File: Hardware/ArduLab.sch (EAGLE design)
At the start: 94 parts, among them CN1 USB-B, CN2 JST-PH, Q1 BSS138, Q2 BSS138, U1 ATMEGA32U4-AU, U2 MIC5205, U3 PAM2401, U4 MCP73831, U5 L293DD, U6 HC_05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

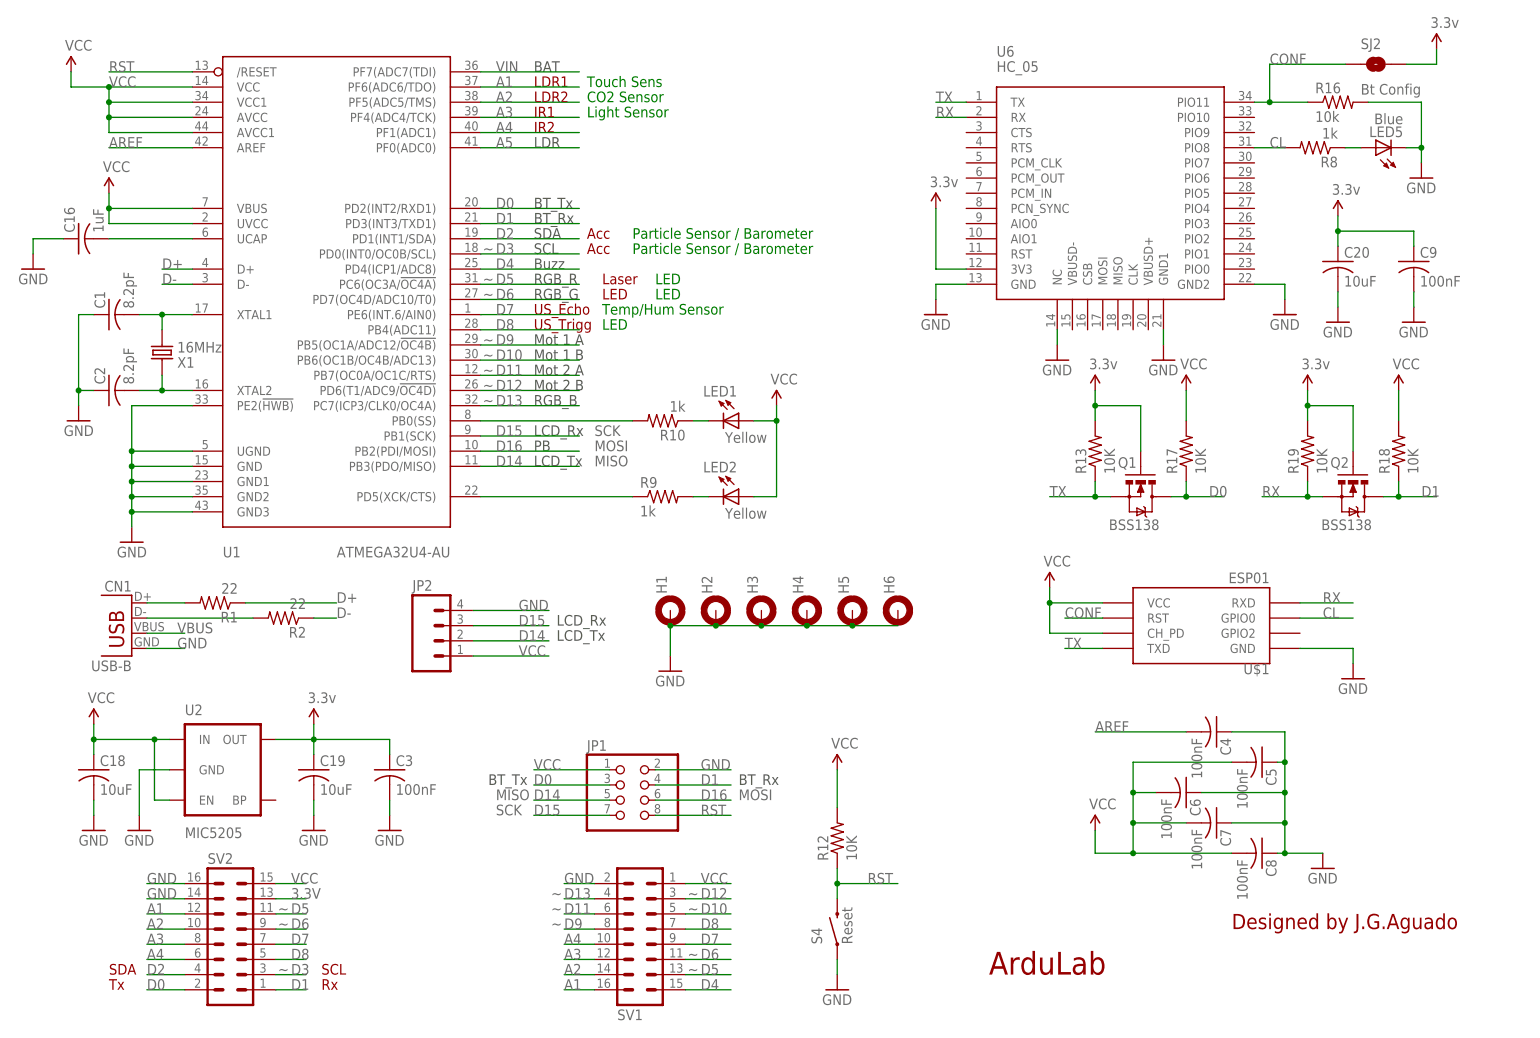
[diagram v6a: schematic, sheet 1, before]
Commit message: 2.4GHz RF ML01D Module Integration
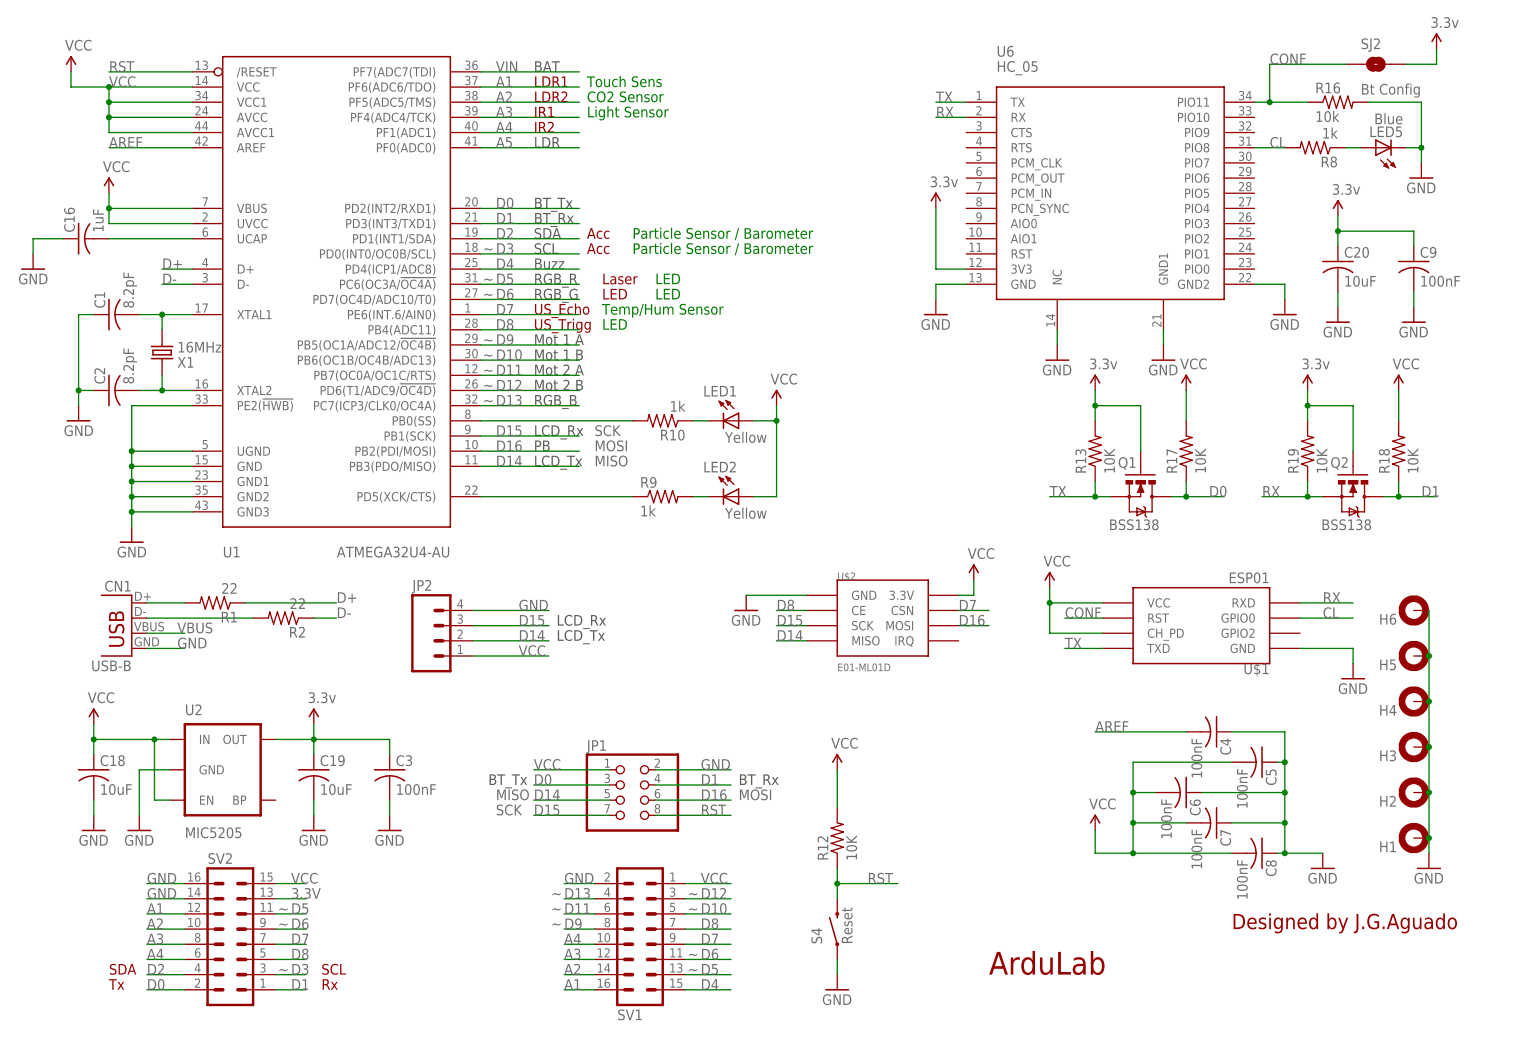
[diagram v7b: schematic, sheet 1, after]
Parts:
- added U$2: E01-ML01D, SpaceDIY_connectors:E01-ML01D
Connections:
- net 3.3V: now also U$2.3.3V
- net D14: now also U$2.MISO
- net D15: now also U$2.SCK
- net D16: now also U$2.MOSI
- net D7: now also U$2.CSN
- net D8: now also U$2.CE
- net GND: now also U$2.GND
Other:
- moved on the sheet: H1, H2, H3, H4, H5, H6
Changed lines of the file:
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@@
 <setting verticaltext="up"/>
 </settings>
-<grid distance="0.1" unitdist="inch" unit="inch" style="lines" multiple="1" display="no" altdistance="0.01" altunitdist="inch" altunit="inch"/>
+<grid distance="0.05" unitdist="inch" unit="inch" style="lines" multiple="1" display="no" altdistance="0.01" altunitdist="inch" altunit="inch"/>
 <layers>
 <layer number="1" name="Top" color="4" fill="1" visible="no" active="no"/>
@@
 <part name="GND5" library="SparkFun" deviceset="GND" device=""/>
 <part name="F1" library="adafruit" deviceset="PTCFUSE" device="-1206" value="500mA"/>
+<part name="GND7" library="SparkFun" deviceset="GND" device=""/>
+<part name="P+12" library="SparkFun" deviceset="3.3V" device="" value="VCC"/>
+<part name="U$2" library="SpaceDIY_connectors" deviceset="E01-ML01D" device=""/>
 </parts>
 <sheets>
@@
 <instance part="R2" gate="G$1" x="57.15" y="72.39" rot="R180"/>
 <instance part="CN1" gate="G$1" x="31.75" y="67.31" rot="MR0"/>
-<instance part="H1" gate="G$1" x="121.92" y="73.66" rot="R90"/>
-<instance part="H2" gate="G$1" x="129.54" y="73.66" rot="R90"/>
-<instance part="H3" gate="G$1" x="137.16" y="73.66" rot="R90"/>
-<instance part="H4" gate="G$1" x="144.78" y="73.66" rot="R90"/>
-<instance part="GND34" gate="1" x="121.92" y="63.5"/>
+<instance part="H1" gate="G$1" x="246.38" y="35.56" rot="R180"/>
+<instance part="H2" gate="G$1" x="246.38" y="43.18" rot="R180"/>
+<instance part="H3" gate="G$1" x="246.38" y="50.8" rot="R180"/>
+<instance part="H4" gate="G$1" x="246.38" y="58.42" rot="R180"/>
+<instance part="GND34" gate="1" x="248.92" y="30.48"/>
 <instance part="R16" gate="G$1" x="233.68" y="158.75"/>
 <instance part="R8" gate="G$1" x="229.87" y="151.13" rot="R180"/>
@@
 <instance part="3.3V4" gate="G$1" x="62.23" y="54.61"/>
 <instance part="P+9" gate="G$1" x="25.4" y="54.61"/>
-<instance part="H5" gate="G$1" x="152.4" y="73.66" rot="R90"/>
-<instance part="H6" gate="G$1" x="160.02" y="73.66" rot="R90"/>
+<instance part="H5" gate="G$1" x="246.38" y="66.04" rot="R180"/>
+<instance part="H6" gate="G$1" x="246.38" y="73.66" rot="R180"/>
 <instance part="C19" gate="G$1" x="62.23" y="46.99"/>
 <instance part="C18" gate="G$1" x="25.4" y="46.99"/>
@@
 <instance part="GND46" gate="1" x="204.47" y="115.57"/>
 <instance part="U1" gate="G$1" x="64.77" y="120.65"/>
+<instance part="GND7" gate="1" x="134.62" y="73.66"/>
+<instance part="P+12" gate="G$1" x="172.72" y="78.74"/>
+<instance part="U$2" gate="G$1" x="157.48" y="66.04"/>
 </instances>
 <busses>
@@
 </segment>
 <segment>
-<wire x1="144.78" y1="71.12" x2="137.16" y2="71.12" width="0.1524" layer="91"/>
-<wire x1="137.16" y1="71.12" x2="129.54" y2="71.12" width="0.1524" layer="91"/>
-<wire x1="129.54" y1="71.12" x2="121.92" y2="71.12" width="0.1524" layer="91"/>
+<wire x1="248.92" y1="58.42" x2="248.92" y2="50.8" width="0.1524" layer="91"/>
+<wire x1="248.92" y1="50.8" x2="248.92" y2="43.18" width="0.1524" layer="91"/>
+<wire x1="248.92" y1="43.18" x2="248.92" y2="35.56" width="0.1524" layer="91"/>
 <pinref part="H1" gate="G$1" pin="MOUNT"/>
-<wire x1="121.92" y1="71.12" x2="121.92" y2="66.04" width="0.1524" layer="91"/>
-<junction x="121.92" y="71.12"/>
+<wire x1="248.92" y1="35.56" x2="248.92" y2="33.02" width="0.1524" layer="91"/>
+<junction x="248.92" y="35.56"/>
 <pinref part="H2" gate="G$1" pin="MOUNT"/>
-<junction x="129.54" y="71.12"/>
+<junction x="248.92" y="43.18"/>
 <pinref part="H3" gate="G$1" pin="MOUNT"/>
-<junction x="137.16" y="71.12"/>
+<junction x="248.92" y="50.8"/>
 <pinref part="H4" gate="G$1" pin="MOUNT"/>
 <pinref part="GND34" gate="1" pin="GND"/>
-<wire x1="160.02" y1="71.12" x2="152.4" y2="71.12" width="0.1524" layer="91"/>
-<wire x1="152.4" y1="71.12" x2="144.78" y2="71.12" width="0.1524" layer="91"/>
+<wire x1="248.92" y1="73.66" x2="248.92" y2="66.04" width="0.1524" layer="91"/>
+<wire x1="248.92" y1="66.04" x2="248.92" y2="58.42" width="0.1524" layer="91"/>
 <pinref part="H5" gate="G$1" pin="MOUNT"/>
-<junction x="152.4" y="71.12"/>
+<junction x="248.92" y="66.04"/>
 <pinref part="H6" gate="G$1" pin="MOUNT"/>
-<junction x="144.78" y="71.12"/>
+<junction x="248.92" y="58.42"/>
 </segment>
 <segment>
@@
 <pinref part="U6" gate="G$1" pin="GND1"/>
 </segment>
+<segment>
+<wire x1="144.78" y1="76.2" x2="134.62" y2="76.2" width="0.1524" layer="91"/>
+<pinref part="GND7" gate="1" pin="GND"/>
+<pinref part="U$2" gate="G$1" pin="GND"/>
+</segment>
 </net>
 <net name="AREF" class="0">
@@
 <pinref part="SV2" gate="G$1" pin="5"/>
 </segment>
+<segment>
+<wire x1="144.78" y1="73.66" x2="139.7" y2="73.66" width="0.1524" layer="91"/>
+<label x="139.7" y="73.66" size="1.778" layer="95"/>
+<pinref part="U$2" gate="G$1" pin="CE"/>
+</segment>
 </net>
 <net name="D9" class="0">
@@
 <pinref part="JP2" gate="G$1" pin="3"/>
 </segment>
+<segment>
+<wire x1="139.7" y1="71.12" x2="144.78" y2="71.12" width="0.1524" layer="91"/>
+<label x="139.7" y="71.12" size="1.778" layer="95"/>
+<pinref part="U$2" gate="G$1" pin="SCK"/>
+</segment>
 </net>
 <net name="D14" class="0">
@@
 <pinref part="JP2" gate="G$1" pin="2"/>
 </segment>
+<segment>
+<wire x1="144.78" y1="68.58" x2="139.7" y2="68.58" width="0.1524" layer="91"/>
+<label x="139.7" y="68.58" size="1.778" layer="95"/>
+<pinref part="U$2" gate="G$1" pin="MISO"/>
+</segment>
 </net>
 <net name="D16" class="0">
@@
 <wire x1="119.38" y1="41.91" x2="132.08" y2="41.91" width="0.1524" layer="91"/>
 <label x="127" y="41.91" size="1.778" layer="95"/>
+</segment>
+<segment>
+<wire x1="170.18" y1="71.12" x2="175.26" y2="71.12" width="0.1524" layer="91"/>
+<label x="170.18" y="71.12" size="1.778" layer="95"/>
+<pinref part="U$2" gate="G$1" pin="MOSI"/>
 </segment>
 </net>
@@
 <label x="58.42" y="17.78" size="1.778" layer="95"/>
 <pinref part="SV2" gate="G$1" pin="7"/>
+</segment>
+<segment>
+<wire x1="170.18" y1="73.66" x2="175.26" y2="73.66" width="0.1524" layer="91"/>
+<label x="170.18" y="73.66" size="1.778" layer="95"/>
+<pinref part="U$2" gate="G$1" pin="CSN"/>
 </segment>
 </net>
@@
 <pinref part="U6" gate="G$1" pin="3V3"/>
 </segment>
-</net>
+<segment>
+<wire x1="172.72" y1="76.2" x2="172.72" y2="78.74" width="0.1524" layer="91"/>
+<pinref part="P+12" gate="G$1" pin="3.3V"/>
+<wire x1="170.18" y1="76.2" x2="172.72" y2="76.2" width="0.1524" layer="91"/>
+<pinref part="U$2" gate="G$1" pin="3.3V"/>
+</segment>
+</net>

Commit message: Updated components silkscreen layout
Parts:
- LED1, LED2, LED3, LED4, LED5: device led:LEDSMT1206 -> SpaceDIY_passive_components:LED1206
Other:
- moved on the sheet: LED1, LED2, LED3, LED4, LED5
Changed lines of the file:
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@@
 <setting verticaltext="up"/>
 </settings>
-<grid distance="0.05" unitdist="inch" unit="inch" style="lines" multiple="1" display="no" altdistance="0.01" altunitdist="inch" altunit="inch"/>
+<grid distance="0.1" unitdist="inch" unit="inch" style="lines" multiple="1" display="no" altdistance="0.01" altunitdist="inch" altunit="inch"/>
 <layers>
 <layer number="1" name="Top" color="4" fill="1" visible="no" active="no"/>
@@
 <part name="R10" library="resistor" deviceset="R-US_" device="R1206" value="1k"/>
 <part name="R9" library="resistor" deviceset="R-US_" device="R1206" value="1k"/>
-<part name="LED1" library="led" deviceset="LED" device="SMT1206" value="Yellow"/>
-<part name="LED2" library="led" deviceset="LED" device="SMT1206" value="Yellow"/>
+<part name="LED1" library="SpaceDIY_passive_components" deviceset="LED1206" device="" value="Yellow"/>
+<part name="LED2" library="SpaceDIY_passive_components" deviceset="LED1206" device="" value="Yellow"/>
 <part name="GND23" library="SparkFun" deviceset="GND" device=""/>
 <part name="GND24" library="SparkFun" deviceset="GND" device=""/>
@@
 <part name="GND16" library="SparkFun" deviceset="GND" device=""/>
 <part name="C22" library="resistor" deviceset="C-US" device="C3216" value="4.7uF"/>
-<part name="LED4" library="led" deviceset="LED" device="SMT1206" value="Yellow"/>
+<part name="LED4" library="SpaceDIY_passive_components" deviceset="LED1206" device="" value="Yellow"/>
 <part name="R6" library="resistor" deviceset="R-US_" device="R1206" value="330"/>
 <part name="GND17" library="SparkFun" deviceset="GND" device=""/>
@@
 <part name="R16" library="resistor" deviceset="R-US_" device="R1206" value="10k"/>
 <part name="R8" library="resistor" deviceset="R-US_" device="R1206" value="1k"/>
-<part name="LED5" library="led" deviceset="LED" device="SMT1206" value="Blue"/>
+<part name="LED5" library="SpaceDIY_passive_components" deviceset="LED1206" device="" value="Blue"/>
 <part name="GND39" library="SparkFun" deviceset="GND" device=""/>
 <part name="SJ2" library="SparkFun-Retired" deviceset="SOLDERJUMPER" device="ROUND" value="Bt Config"/>
@@
 <part name="C17" library="resistor" deviceset="C-US" device="C1206" value="22uF"/>
 <part name="C21" library="resistor" deviceset="C-US" device="C1206" value="22uF"/>
-<part name="LED3" library="led" deviceset="LED" device="SMT1206" value="Green"/>
+<part name="LED3" library="SpaceDIY_passive_components" deviceset="LED1206" device="" value="Green"/>
 <part name="GND13" library="SparkFun-PowerSymbols" deviceset="GND" device=""/>
 <part name="SV2" library="con-lstb" deviceset="MA08-2" device=""/>
@@
 <instance part="R10" gate="G$1" x="120.65" y="105.41" rot="R180"/>
 <instance part="R9" gate="G$1" x="120.65" y="92.71"/>
-<instance part="LED1" gate="G$1" x="133.35" y="105.41" smashed="yes" rot="R270">
-<attribute name="NAME" x="133.096" y="111.252" size="1.778" layer="95" rot="R180"/>
-<attribute name="VALUE" x="131.064" y="101.727" size="1.778" layer="96"/>
+<instance part="LED1" gate="G$1" x="130.81" y="105.41" smashed="yes" rot="R180">
+<attribute name="NAME" x="136.652" y="105.664" size="1.778" layer="95" rot="R90"/>
+<attribute name="VALUE" x="127.127" y="107.696" size="1.778" layer="96" rot="R270"/>
 </instance>
-<instance part="LED2" gate="G$1" x="133.35" y="92.71" smashed="yes" rot="R270">
-<attribute name="NAME" x="133.096" y="98.552" size="1.778" layer="95" rot="R180"/>
-<attribute name="VALUE" x="131.064" y="89.027" size="1.778" layer="96"/>
+<instance part="LED2" gate="G$1" x="130.81" y="92.71" smashed="yes" rot="R180">
+<attribute name="NAME" x="136.652" y="92.964" size="1.778" layer="95" rot="R90"/>
+<attribute name="VALUE" x="127.127" y="94.996" size="1.778" layer="96" rot="R270"/>
 </instance>
 <instance part="GND23" gate="1" x="31.75" y="85.09" rot="MR0"/>
@@
 <instance part="R16" gate="G$1" x="233.68" y="158.75"/>
 <instance part="R8" gate="G$1" x="229.87" y="151.13" rot="R180"/>
-<instance part="LED5" gate="G$1" x="240.03" y="151.13" rot="R90"/>
+<instance part="LED5" gate="G$1" x="242.57" y="151.13"/>
 <instance part="GND39" gate="1" x="247.65" y="146.05"/>
 <instance part="SJ2" gate="1" x="240.03" y="165.1"/>
@@
 <instance part="GND16" gate="1" x="78.74" y="148.59"/>
 <instance part="C22" gate="G$1" x="20.32" y="153.67"/>
-<instance part="LED4" gate="G$1" x="29.21" y="156.21"/>
+<instance part="LED4" gate="G$1" x="29.21" y="153.67" rot="R270"/>
 <instance part="R6" gate="G$1" x="35.56" y="149.86" rot="R180"/>
 <instance part="GND17" gate="1" x="20.32" y="139.7"/>
@@
 <instance part="C17" gate="G$1" x="198.12" y="146.05" rot="R180"/>
 <instance part="C21" gate="G$1" x="208.28" y="146.05" rot="R180"/>
-<instance part="LED3" gate="G$1" x="101.6" y="124.46"/>
+<instance part="LED3" gate="G$1" x="101.6" y="121.92" rot="R270"/>
 <instance part="GND13" gate="1" x="227.33" y="138.43"/>
 <instance part="D3" gate="G$1" x="88.9" y="129.54"/>
